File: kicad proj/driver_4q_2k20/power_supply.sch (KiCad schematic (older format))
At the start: 18 parts, among them T1 Transformer, U3 MAX17634C, U4 AC_Con

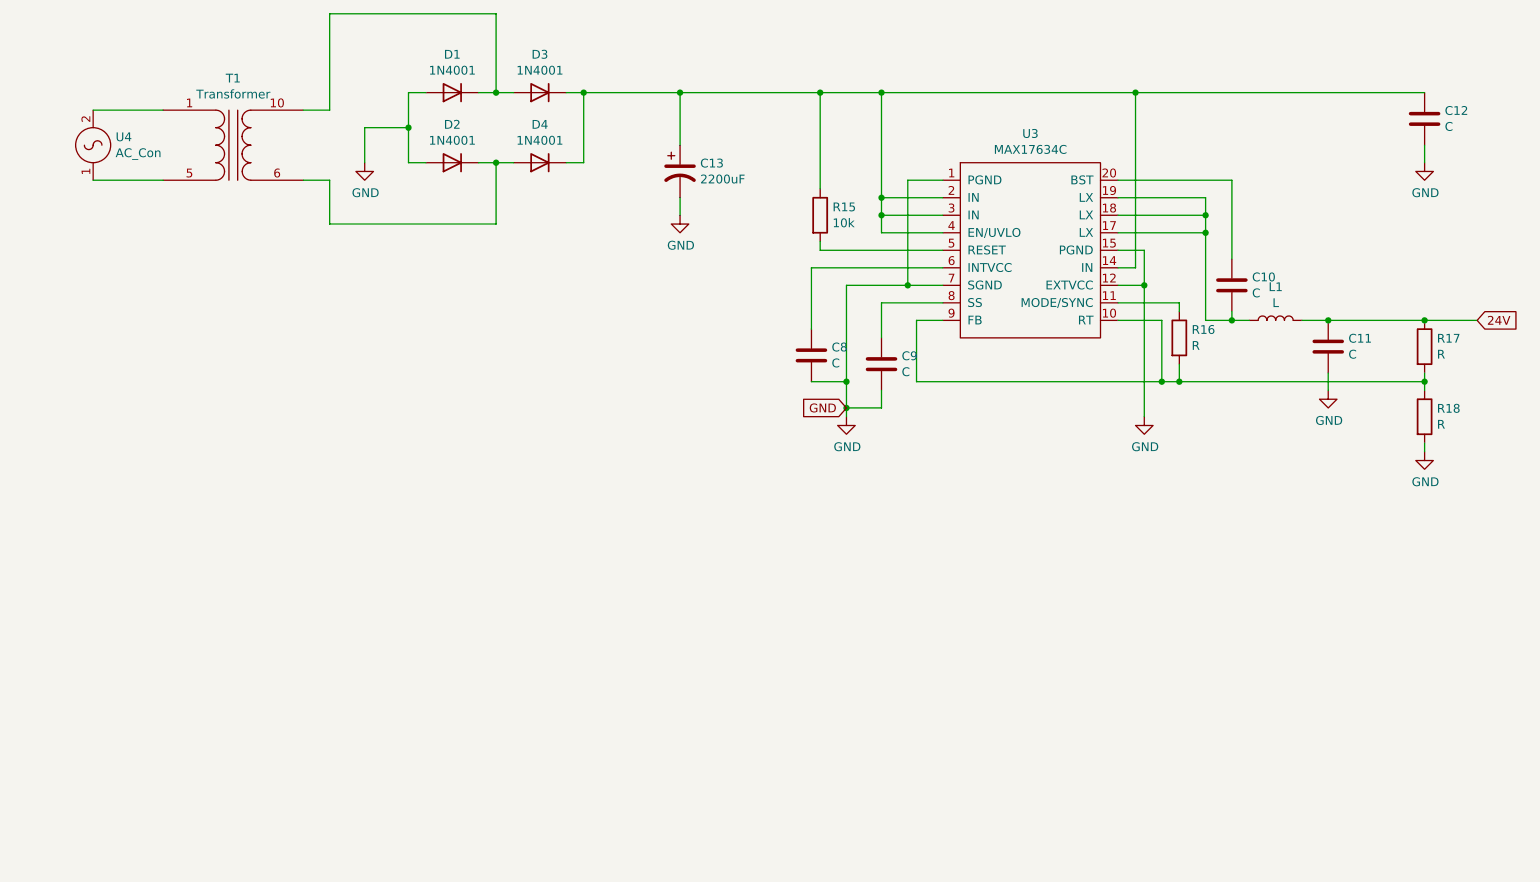
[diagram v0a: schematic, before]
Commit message: added power supply and new transformer
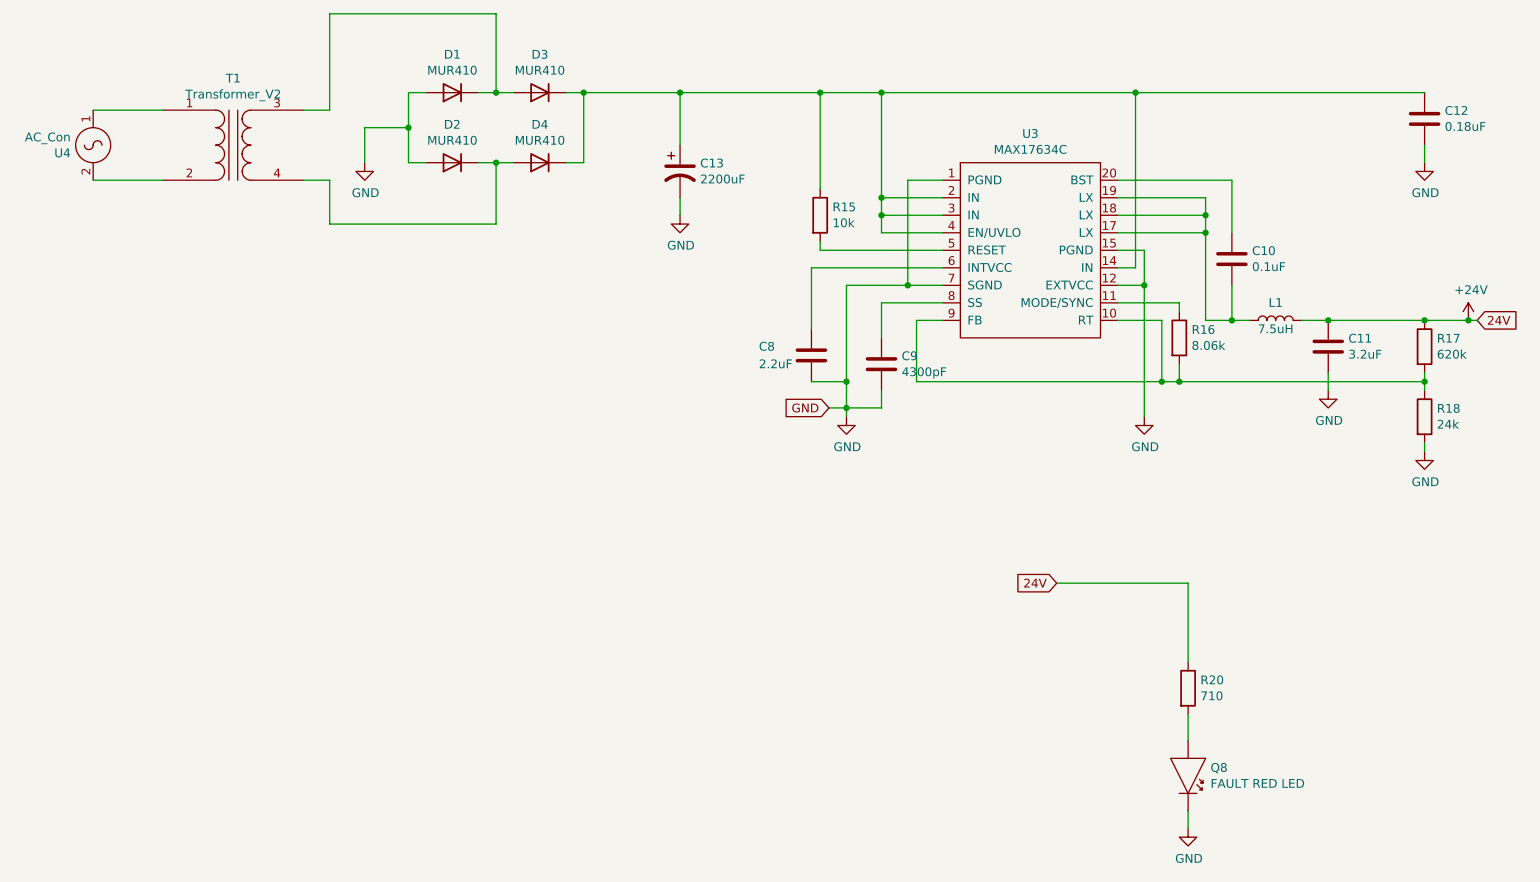
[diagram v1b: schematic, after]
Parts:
- removed T1: Transformer, driver_4q_2k20:Transformer_Breve_TEZ-28x33, symbol driver_4q_2k20_lib:Transformer
- added Q8: FAULT RED LED, driver_4q_2k20:LTL-10224W-RED, symbol driver_4q_2k20_lib:LED
- added R20: 710, driver_4q_2k20:C_0402_1005Metric, symbol Device:R
- added T1: Transformer_V2, driver_4q_2k20:Transformer_96x87, symbol driver_4q_2k20_lib:Transformer_V2
- C10: value C -> 0.1uF
- C11: value C -> 3.2uF
- C12: value C -> 0.18uF
- C8: value C -> 2.2uF
- C9: value C -> 4300pF
- D1, D2, D3, D4: value 1N4001 -> MUR410
- L1: value L -> 7.5uH; footprint (none) -> driver_4q_2k20:L_TracoPower_TCK-047_5.2x5.8mm
- R16: value R -> 8.06k
- R17: value R -> 620k
- R18: value R -> 24k
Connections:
- net GND: now also Q8.2
- net at D1.1 (K), D3.2 (A): now also T1.3 (SB)
- net at U4.1: now also T1.1 (AA)
- net at U4.2: now also T1.2 (AB)
- net at D2.1 (K), D4.2 (A): now also T1.4 (SA)
- net 24V renamed +24V
- net +24V: now also R20.1
- new net: Q8.1 (K), R20.2
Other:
- moved on the sheet: C10
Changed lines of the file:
@@
 P 8650 1550
 F 0 "C12" H 8765 1596 50  0000 L CNN
-F 1 "C" H 8765 1505 50  0000 L CNN
+F 1 "0.18uF" H 8765 1505 50  0000 L CNN
 F 2 "driver_4q_2k20:C_0402_1005Metric" H 8688 1400 50  0001 C CNN
-F 3 "~" H 8650 1550 50  0001 C CNN
+F 3 "http://www.farnell.com/datasheets/2740606.pdf?_ga=2.113568463.958972427.1592861482-895881421.1592861482" H 8650 1550 50  0001 C CNN
 	1    8650 1550
 	1    0    0    -1
@@
 L Device:C C10
 U 1 1 5EEE0240
-P 7550 2500
-F 0 "C10" H 7665 2546 50  0000 L CNN
-F 1 "C" H 7665 2455 50  0000 L CNN
-F 2 "driver_4q_2k20:C_0402_1005Metric" H 7588 2350 50  0001 C CNN
-F 3 "~" H 7550 2500 50  0001 C CNN
-	1    7550 2500
+P 7550 2350
+F 0 "C10" H 7665 2396 50  0000 L CNN
+F 1 "0.1uF" H 7665 2305 50  0000 L CNN
+F 2 "driver_4q_2k20:C_0402_1005Metric" H 7588 2200 50  0001 C CNN
+F 3 "~" H 7550 2350 50  0001 C CNN
+	1    7550 2350
 	1    0    0    -1
 $EndComp
 Wire Wire Line
 	6900 1900 7550 1900
-$Comp
-L Device:L L1
-U 1 1 5EEE1312
-P 7800 2700
-F 0 "L1" V 7990 2700 50  0000 C CNN
-F 1 "L" V 7899 2700 50  0000 C CNN
-F 2 "" H 7800 2700 50  0001 C CNN
-F 3 "~" H 7800 2700 50  0001 C CNN
-	1    7800 2700
-	0    -1   -1   0
-$EndComp
-Wire Wire Line
-	7550 2650 7550 2700
 Wire Wire Line
 	7550 2700 7650 2700
-Wire Wire Line
-	7550 1900 7550 2350
 Wire Wire Line
 	6900 2000 7400 2000
@@
 P 8100 2850
 F 0 "C11" H 8215 2896 50  0000 L CNN
-F 1 "C" H 8215 2805 50  0000 L CNN
+F 1 "3.2uF" H 8215 2805 50  0000 L CNN
 F 2 "driver_4q_2k20:C_0402_1005Metric" H 8138 2700 50  0001 C CNN
 F 3 "~" H 8100 2850 50  0001 C CNN
@@
 P 8650 2850
 F 0 "R17" H 8720 2896 50  0000 L CNN
-F 1 "R" H 8720 2805 50  0000 L CNN
+F 1 "620k" H 8720 2805 50  0000 L CNN
 F 2 "driver_4q_2k20:R_0402_1005Metric" V 8580 2850 50  0001 C CNN
 F 3 "~" H 8650 2850 50  0001 C CNN
@@
 P 8650 3250
 F 0 "R18" H 8720 3296 50  0000 L CNN
-F 1 "R" H 8720 3205 50  0000 L CNN
+F 1 "24k" H 8720 3205 50  0000 L CNN
 F 2 "driver_4q_2k20:R_0402_1005Metric" V 8580 3250 50  0001 C CNN
 F 3 "~" H 8650 3250 50  0001 C CNN
@@
 P 5550 2950
 F 0 "C9" H 5665 2996 50  0000 L CNN
-F 1 "C" H 5665 2905 50  0000 L CNN
+F 1 "4300pF" H 5665 2905 50  0000 L CNN
 F 2 "driver_4q_2k20:C_0402_1005Metric" H 5588 2800 50  0001 C CNN
-F 3 "~" H 5550 2950 50  0001 C CNN
+F 3 "http://www.farnell.com/datasheets/2740912.pdf?_ga=2.156084723.958972427.1592861482-895881421.1592861482" H 5550 2950 50  0001 C CNN
 	1    5550 2950
 	1    0    0    -1
@@
 U 1 1 5EEF48FF
 P 5150 2900
-F 0 "C8" H 5265 2946 50  0000 L CNN
-F 1 "C" H 5265 2855 50  0000 L CNN
+F 0 "C8" H 4850 2950 50  0000 L CNN
+F 1 "2.2uF" H 4850 2850 50  0000 L CNN
 F 2 "driver_4q_2k20:C_0402_1005Metric" H 5188 2750 50  0001 C CNN
 F 3 "~" H 5150 2900 50  0001 C CNN
@@
 P 7250 2800
 F 0 "R16" H 7320 2846 50  0000 L CNN
-F 1 "R" H 7320 2755 50  0000 L CNN
+F 1 "8.06k" H 7320 2755 50  0000 L CNN
 F 2 "driver_4q_2k20:R_0402_1005Metric" V 7180 2800 50  0001 C CNN
 F 3 "~" H 7250 2800 50  0001 C CNN
@@
 24V
 Wire Wire Line
-	8650 2700 8950 2700
+	8650 2700 8900 2700
 Connection ~ 8650 2700
-Text GLabel 5350 3200 0    50   Input ~ 0
+Text GLabel 5250 3200 0    50   Input ~ 0
 GND
 Wire Wire Line
@@
 L driver_4q_2k20_lib:AC_Con U4
 U 1 1 5EF5F31F
-P 1050 1350
-F 0 "U4" H 1178 1046 50  0000 L CNN
-F 1 "AC_Con" H 1178 955 50  0000 L CNN
-F 2 "driver_4q_2k20:395430203" H 1150 1250 50  0001 C CNN
-F 3 "" H 1150 1250 50  0001 C CNN
-	1    1050 1350
-	1    0    0    -1
+P 1050 2050
+F 0 "U4" H 1178 1746 50  0000 L CNN
+F 1 "AC_Con" H 1178 1655 50  0000 L CNN
+F 2 "driver_4q_2k20:395430203" H 1150 1950 50  0001 C CNN
+F 3 "" H 1150 1950 50  0001 C CNN
+	1    1050 2050
+	-1   0    0    1
 $EndComp
 Wire Wire Line
@@
 P 3100 1400
 F 0 "D1" H 3100 1183 50  0000 C CNN
-F 1 "1N4001" H 3100 1274 50  0000 C CNN
+F 1 "MUR410" H 3100 1274 50  0000 C CNN
 F 2 "driver_4q_2k20:D_DO-41_SOD81_P10.16mm_Horizontal" H 3100 1400 50  0001 C CNN
-F 3 "~" H 3100 1400 50  0001 C CNN
+F 3 "https://www.onsemi.com/pub/Collateral/MUR420-D.PDF" H 3100 1400 50  0001 C CNN
 	1    3100 1400
 	-1   0    0    1
@@
 Connection ~ 4400 1400
 $Comp
+L Device:D D3
+U 1 1 5EF1C06D
+P 3600 1400
+F 0 "D3" H 3600 1183 50  0000 C CNN
+F 1 "MUR410" H 3600 1274 50  0000 C CNN
+F 2 "driver_4q_2k20:D_DO-41_SOD81_P10.16mm_Horizontal" H 3600 1400 50  0001 C CNN
+F 3 "https://www.onsemi.com/pub/Collateral/MUR420-D.PDF" H 3600 1400 50  0001 C CNN
+	1    3600 1400
+	-1   0    0    1
+$EndComp
+$Comp
+L Device:D D4
+U 1 1 5EF1E8C5
+P 3600 1800
+F 0 "D4" H 3600 1583 50  0000 C CNN
+F 1 "MUR410" H 3600 1674 50  0000 C CNN
+F 2 "driver_4q_2k20:D_DO-41_SOD81_P10.16mm_Horizontal" H 3600 1800 50  0001 C CNN
+F 3 "https://www.onsemi.com/pub/Collateral/MUR420-D.PDF" H 3600 1800 50  0001 C CNN
+	1    3600 1800
+	-1   0    0    1
+$EndComp
+$Comp
 L Device:D D2
-U 1 1 5EFD0AB7
+U 1 1 5EF2115E
 P 3100 1800
 F 0 "D2" H 3100 1583 50  0000 C CNN
-F 1 "1N4001" H 3100 1674 50  0000 C CNN
+F 1 "MUR410" H 3100 1674 50  0000 C CNN
 F 2 "driver_4q_2k20:D_DO-41_SOD81_P10.16mm_Horizontal" H 3100 1800 50  0001 C CNN
-F 3 "~" H 3100 1800 50  0001 C CNN
+F 3 "https://www.onsemi.com/pub/Collateral/MUR420-D.PDF" H 3100 1800 50  0001 C CNN
 	1    3100 1800
 	-1   0    0    1
 $EndComp
-$Comp
-L Device:D D3
-U 1 1 5EFD33E6
-P 3600 1400
-F 0 "D3" H 3600 1183 50  0000 C CNN
-F 1 "1N4001" H 3600 1274 50  0000 C CNN
-F 2 "driver_4q_2k20:D_DO-41_SOD81_P10.16mm_Horizontal" H 3600 1400 50  0001 C CNN
-F 3 "~" H 3600 1400 50  0001 C CNN
-	1    3600 1400
-	-1   0    0    1
-$EndComp
-$Comp
-L Device:D D4
-U 1 1 5EFD5B58
-P 3600 1800
-F 0 "D4" H 3600 1583 50  0000 C CNN
-F 1 "1N4001" H 3600 1674 50  0000 C CNN
-F 2 "driver_4q_2k20:D_DO-41_SOD81_P10.16mm_Horizontal" H 3600 1800 50  0001 C CNN
-F 3 "~" H 3600 1800 50  0001 C CNN
-	1    3600 1800
-	-1   0    0    1
-$EndComp
-$Comp
-L driver_4q_2k20_lib:Transformer T1
-U 1 1 5EFFBB25
+Wire Wire Line
+	5250 3200 5350 3200
+$Comp
+L Device:L L1
+U 1 1 5EEE1312
+P 7800 2700
+F 0 "L1" V 7900 2700 50  0000 C CNN
+F 1 "7.5uH" V 7750 2700 50  0000 C CNN
+F 2 "driver_4q_2k20:L_TracoPower_TCK-047_5.2x5.8mm" H 7800 2700 50  0001 C CNN
+F 3 "https://br.mouser.com/datasheet/2/54/SDR0603-1391338.pdf" H 7800 2700 50  0001 C CNN
+	1    7800 2700
+	0    -1   -1   0
+$EndComp
+Wire Wire Line
+	7550 2200 7550 1900
+Wire Wire Line
+	7550 2500 7550 2700
+$Comp
+L driver_4q_2k20_lib:Transformer_V2 T1
+U 1 1 5EF3CAFE
 P 1850 1700
 F 0 "T1" H 1850 2081 50  0000 C CNN
-F 1 "Transformer" H 1850 1990 50  0000 C CNN
-F 2 "driver_4q_2k20:Transformer_Breve_TEZ-28x33" H 1850 1700 50  0001 C CNN
-F 3 "~" H 1850 1700 50  0001 C CNN
+F 1 "Transformer_V2" H 1850 1990 50  0000 C CNN
+F 2 "driver_4q_2k20:Transformer_96x87" H 1850 2050 50  0001 C CNN
+F 3 "https://produto.mercadolivre.com.br/MLB-1380978889-transformador-3030v-5a-trafo-bivolt-_JM?matt_tool=82322591&matt_word&gclid=CjwKCAjwrcH3BRApEiwAxjdPTe2Vd3MLpWKpp-Edq8fe_aW-2E-paqNDO8qglkeG-WZi5CFErjztdRoCUE4QAvD_BwE&quantity=1" H 1850 1700 50  0001 C CNN
 	1    1850 1700
 	1    0    0    -1
 $EndComp
+$Comp
+L power:+24V #PWR0106
+U 1 1 5EF5E6CD
+P 8900 2700
+F 0 "#PWR0106" H 8900 2550 50  0001 C CNN
+F 1 "+24V" H 8915 2873 50  0000 C CNN
+F 2 "" H 8900 2700 50  0001 C CNN
+F 3 "" H 8900 2700 50  0001 C CNN
+	1    8900 2700
+	1    0    0    -1
+$EndComp
+Connection ~ 8900 2700
+Wire Wire Line
+	8900 2700 8950 2700
+Text GLabel 6550 4200 0    50   Input ~ 0
+24V
+Wire Wire Line
+	7300 5500 7300 5600
+$Comp
+L power:GND #PWR?
+U 1 1 5EF6ADA5
+P 7300 5600
+AR Path="/5EF6ADA5" Ref="#PWR?"  Part="1"
+AR Path="/5EE6A706/5EF6ADA5" Ref="#PWR?"  Part="1"
+AR Path="/5EDE0D36/5EF6ADA5" Ref="#PWR025"  Part="1"
+F 0 "#PWR025" H 7300 5350 50  0001 C CNN
+F 1 "GND" H 7305 5427 50  0000 C CNN
+F 2 "" H 7300 5600 50  0001 C CNN
+F 3 "" H 7300 5600 50  0001 C CNN
+	1    7300 5600
+	1    0    0    -1
+$EndComp
+$Comp
+L driver_4q_2k20_lib:LED Q?
+U 1 1 5EF6ADB3
+P 7550 5200
+AR Path="/5EF6ADB3" Ref="Q?"  Part="1"
+AR Path="/5EE6A706/5EF6ADB3" Ref="Q?"  Part="1"
+AR Path="/5EDE0D36/5EF6ADB3" Ref="Q8"  Part="1"
+F 0 "Q8" V 7604 5078 50  0000 L CNN
+F 1 "FAULT RED LED" V 7695 5078 50  0000 L CNN
+F 2 "driver_4q_2k20:LTL-10224W-RED" H 7550 5200 50  0001 C CNN
+F 3 "https://www.mouser.com/datasheet/2/239/lite-on_lite-s-a0003556554-1-1737487.pdf" H 7550 5200 50  0001 C CNN
+	1    7550 5200
+	0    1    1    0
+$EndComp
+$Comp
+L Device:R R?
+U 1 1 5EF6ADBD
+P 7300 4800
+AR Path="/5EF6ADBD" Ref="R?"  Part="1"
+AR Path="/5EE6A706/5EF6ADBD" Ref="R?"  Part="1"
+AR Path="/5EDE0D36/5EF6ADBD" Ref="R20"  Part="1"
+F 0 "R20" H 7370 4846 50  0000 L CNN
+F 1 "710" H 7370 4755 50  0000 L CNN
+F 2 "driver_4q_2k20:C_0402_1005Metric" V 7230 4800 50  0001 C CNN
+F 3 "~" H 7300 4800 50  0001 C CNN
+	1    7300 4800
+	1    0    0    -1
+$EndComp
+Wire Wire Line
+	6550 4200 7300 4200
+Wire Wire Line
+	7300 4200 7300 4650
+Wire Wire Line
+	7300 4950 7300 5100
 $EndSCHEMATC
